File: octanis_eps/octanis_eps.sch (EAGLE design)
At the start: 167 parts, among them IC10 OPA2333DGK, IC11 OPA2333DGK, IC12 OPA2333DGK, IC2 OPA2333DGK, IC3 OPA2333DGK, IC4 OPA2333DGK, IC5 OPA2333DGK, IC6 OPA2333DGK, IC7 OPA2333DGK, IC8 OPA2333DGK, IC9 OPA2333DGK, Q1 FC-12M

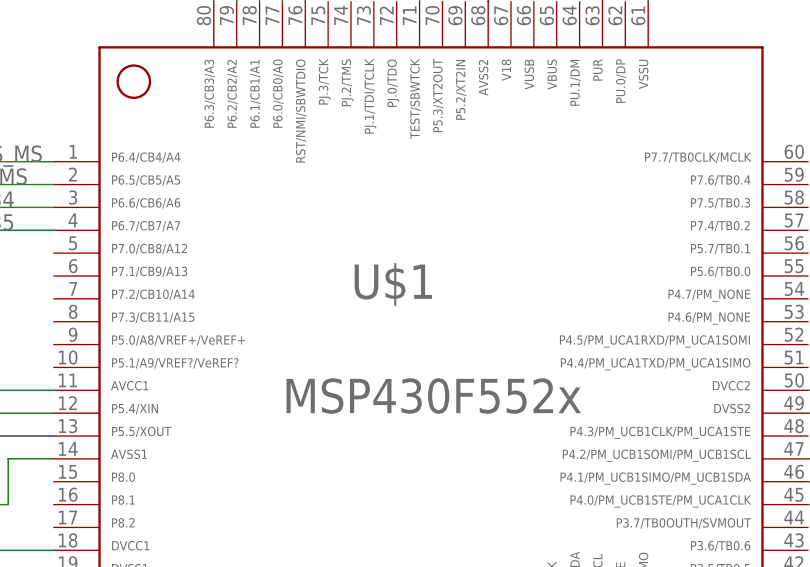
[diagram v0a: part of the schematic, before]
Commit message: replaced the msp430 to the same component like in the octanis 0.1 board
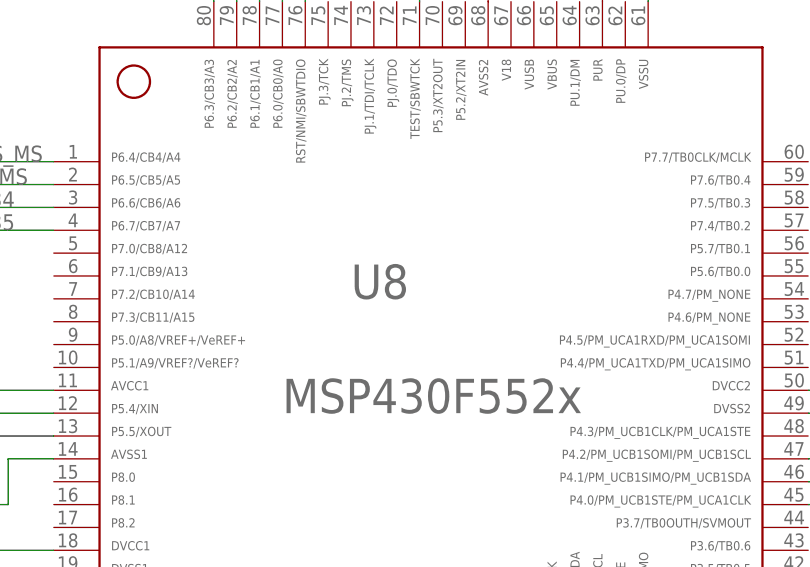
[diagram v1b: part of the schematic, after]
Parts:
- removed U$1: F552X---PN80, TI_MSP430_v16:F552X---PN80
- added U8: MSP430F5529IPNR, TI_MSP430_v16_intern:F552X---PN80
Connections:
- net +3V3: now also U8.14, U8.18, U8.50; no longer U$1.14, U$1.18, U$1.50
- net GND: now also U8.19, U8.49, U8.61, U8.68; no longer U$1.19, U$1.49, U$1.61, U$1.68
- net I2C_SCL: now also U8.47; no longer U$1.47
- net I2C_SDA: now also U8.46; no longer U$1.46
- net I_BOT_MS: now also U8.78; no longer U$1.78
- net I_CHG_MS: now also U8.79; no longer U$1.79
- net I_DSG_MS: now also U8.80; no longer U$1.80
- net I_TOP_MS: now also U8.77; no longer U$1.77
- net N$27: now also U8.63; no longer U$1.63
- net N$28: now also U8.45; no longer U$1.45
- net N$34: now also U8.3; no longer U$1.3
- net N$35: now also U8.4; no longer U$1.4
- net N$48: now also U8.12; no longer U$1.12
- net N$49: now also U8.20; no longer U$1.20
- net N$50: now also U8.13; no longer U$1.13
- net RST/SBWTDIO: now also U8.76; no longer U$1.76
- net TEST/SBWTCK: now also U8.71; no longer U$1.71
- net VCC: now also U8.11; no longer U$1.11
- net V_BT_MS: now also U8.2; no longer U$1.2
- net V_BUS_MS: now also U8.1; no longer U$1.1

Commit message: eps board save Thu-22-01-2015
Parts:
- removed JP2, JP3, JP4, JP5: (no value), jumper:JP1E
- removed U8: MSP430F5529IPNR, TI_MSP430_v16_intern:F552X---PN80
- added A_EXT, PW_EXT3, SC_JMPR: (no value), jumper:JP4E
- added U$1: F552X---PN80, TI_MSP430_v16:F552X---PN80
- added U$16, U$17, U$18: TPS2022D, Octanis1_EPS:TPS2022D
- renumbered EXT1 to PW_EXT1, EXT2 to PW_EXT2, JP1 to I2C
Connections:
- removed net I_BOT_MS: IC3B.-IN, IC3B.OUT, U8.78
- removed net I_TOP_MS: IC3A.-IN, IC3A.OUT, U8.77
- removed net N$35: U8.4
- removed net SC+_BOT: R8.1, SC_BOT.1, SC_BOT.2, U$2.RS+
- removed net SC+_TOP: R6.1, SC_TOP.1, SC_TOP.2, U$3.RS+
- new net AEXT4: A_EXT.1, U$1.6
- new net A_EXT1: A_EXT.4, U$1.3
- new net A_EXT2: A_EXT.3, U$1.4
- new net A_EXT3: A_EXT.2, U$1.5
- new net EN_EXT1: U$1.57, U$13.G
- new net EN_EXT2: U$1.58, U$15.G
- new net EN_EXT3: U$1.59, U$14.G
- new net EXT3+: PW_EXT3.3, PW_EXT3.4, U$18.OUT1, U$18.OUT2, U$18.OUT3
- new net EXT_PW: C26.+, C27.+, C28.+, C29.2, C30.2, C31.2, R6.2, U$16.IN1, U$16.IN2, U$17.IN1, U$17.IN2, U$18.IN1, U$18.IN2, U$3.RS-
- new net I_EXT_PW: IC3A.-IN, IC3A.OUT, U$1.78
- new net I_SC: IC3B.-IN, IC3B.OUT, U$1.77
- new net N$79: U$13.D, U$16.EN
- new net N$80: U$14.D, U$18.EN
- new net SC+: R8.1, SC_BOT.1, SC_BOT.2, SC_TOP.1, SC_TOP.2, U$2.RS+
- new net SC-: SC_BOT.3, SC_BOT.4, SC_JMPR.2, SC_JMPR.4, SC_TOP.3, SC_TOP.4
- net +3V3: now also U$1.14, U$1.18, U$1.50; no longer U8.14, U8.18, U8.50
- net EXT1+: now also U$16.OUT1, U$16.OUT2, U$16.OUT3
- net EXT2+: now also U$17.OUT1, U$17.OUT2, U$17.OUT3
- net GND: now also C26.-, C27.-, C28.-, C29.1, C30.1, C31.1, PW_EXT3.1, PW_EXT3.2, SC_JMPR.1, SC_JMPR.3, U$1.19, U$1.49, U$1.61, U$1.68, U$16.GND, U$17.GND, U$18.GND; no longer SC_BOT.3, SC_BOT.4, SC_TOP.3, SC_TOP.4, U8.19, U8.49, U8.61, U8.68
- net I2C_SCL: now also U$1.47; no longer U8.47
- net I2C_SDA: now also U$1.46; no longer U8.46
- net I_CHG_MS: now also U$1.79; no longer U8.79
- net I_DSG_MS: now also U$1.80; no longer U8.80
- net N$27: now also U$1.63; no longer U8.63
- net N$28: now also U$1.45; no longer U8.45
- net N$34: now also U$15.D, U$17.EN; no longer U8.3
- net N$48: now also U$1.12; no longer U8.12
- net N$49: now also U$1.20; no longer U8.20
- net N$50: now also U$1.13; no longer U8.13
- net RST/SBWTDIO: now also U$1.76; no longer U8.76
- net TEST/SBWTCK: now also U$1.71; no longer U8.71
- net VCC: now also R6.1, U$1.11, U$3.RS+; no longer R6.2, U$3.RS-, U8.11
- net V_BT_MS: now also U$1.2; no longer U8.2
- net V_BUS_MS: now also U$1.1; no longer U8.1
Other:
- note added: "External consumption"
- note added: "External mod 3"
- note added: "External switches (<1.5A)"
- note added: "SOLAR Cells"
- note added: "connect SC jumper"
- note removed: "External switches"
- note removed: "TOP_SC"
- moved on the sheet: BT_IN, BT_JMPR, C28, C31, U$14
